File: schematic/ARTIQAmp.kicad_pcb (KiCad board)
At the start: 8 copper layers, 191 x 152.4 mm, 393 parts, among them IC1 LTC6090CS8E#PBF, IC10 LTC6090CS8E#PBF, IC11 LTC6090CS8E#PBF, IC12 LTC6090CS8E#PBF, IC13 LTC6090CS8E#PBF, IC14 LTC6090CS8E#PBF, IC15 LTC6090CS8E#PBF, IC16 LTC6090CS8E#PBF, IC17 LTC6090CS8E#PBF, IC18 LTC6090CS8E#PBF, IC19 LTC6090CS8E#PBF, IC2 LTC6090CS8E#PBF, IC20 LTC6090CS8E#PBF, IC21 LTC6090CS8E#PBF, IC22 LTC6090CS8E#PBF, IC23 LTC6090CS8E#PBF, IC24 LTC6090CS8E#PBF, IC25 LTC6090CS8E#PBF, IC26 LTC6090CS8E#PBF, IC27 LTC6090CS8E#PBF, IC28 LTC6090CS8E#PBF, IC29 LTC6090CS8E#PBF, IC3 LTC6090CS8E#PBF, IC30 LTC6090CS8E#PBF, IC31 LTC6090CS8E#PBF, IC32 LTC6090CS8E#PBF, IC4 LTC6090CS8E#PBF, IC5 LTC6090CS8E#PBF, IC6 LTC6090CS8E#PBF, IC7 LTC6090CS8E#PBF, IC8 LTC6090CS8E#PBF, IC9 LTC6090CS8E#PBF, J1 Power conneciton, J2 HD68, J3 HD68

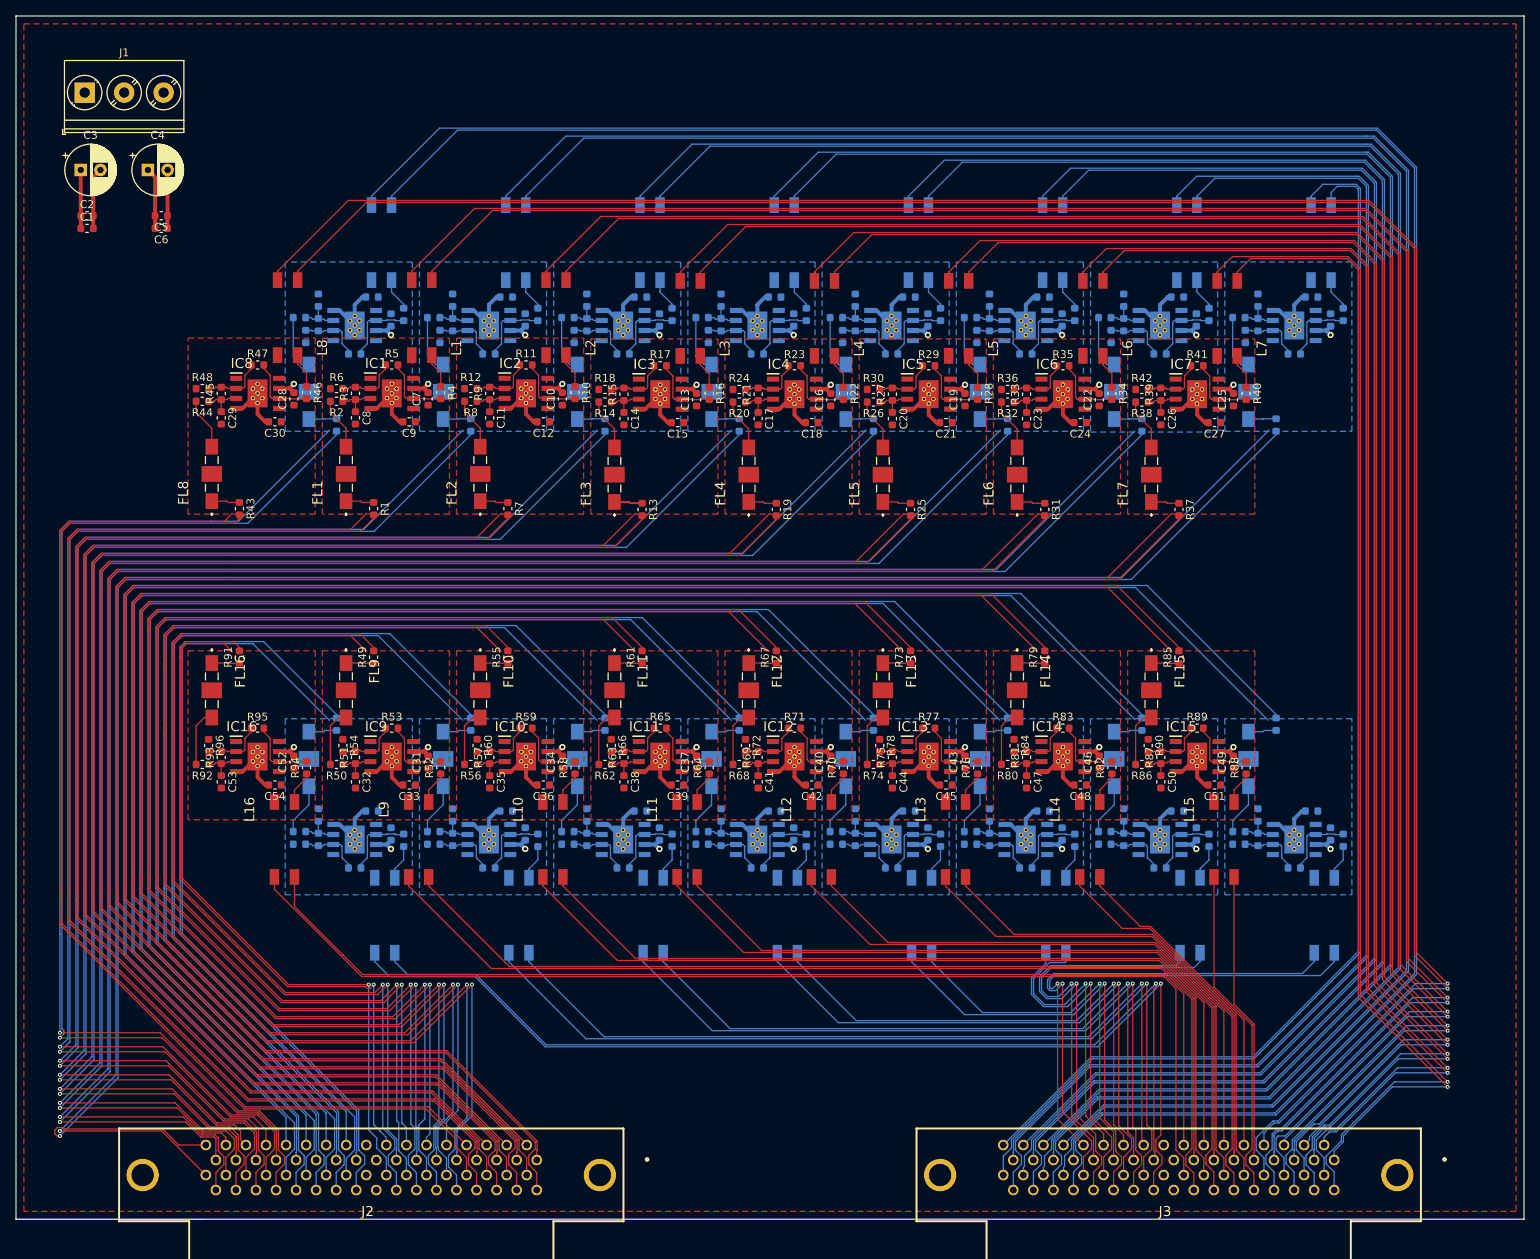
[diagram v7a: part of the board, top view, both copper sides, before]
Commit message: Board updates and starting to add more capacitors
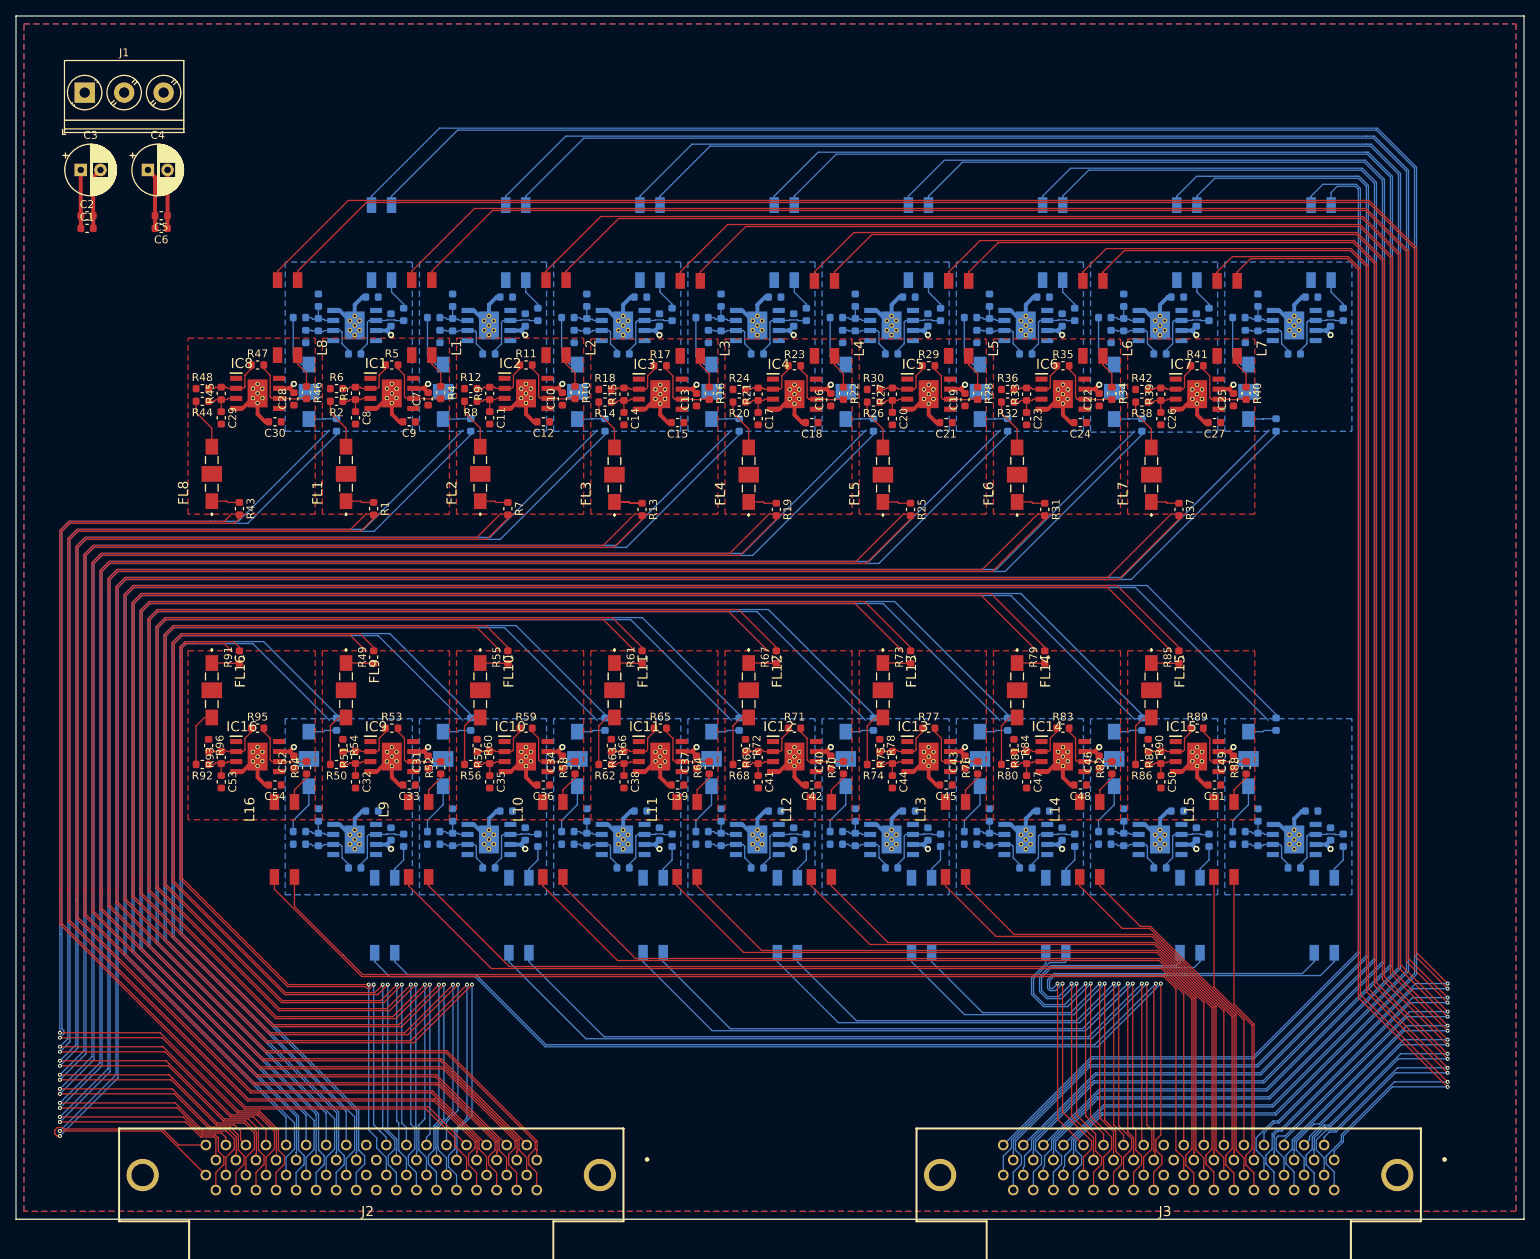
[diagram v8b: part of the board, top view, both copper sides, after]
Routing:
- added copper zone on B.Cu, net GND
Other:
- copper layers 8 -> 6
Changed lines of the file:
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@@
     (0 F.Cu signal)
     (1 In1.Cu power)
-    (2 In24.Cu signal)
-    (3 In2.Cu power)
-    (4 In3.Cu power)
-    (5 In54.Cu signal)
-    (6 In4.Cu power)
+    (2 In2.Cu power)
+    (3 In3.Cu power)
+    (4 In4.Cu power)
     (31 B.Cu signal)
     (32 B.Adhes user)
@@
   )
   (zone (net 198) (net_name /D25_IN_COM) (layer B.Cu) (hatch edge 0.508)
+    (priority 1)
     (connect_pads yes (clearance 0.254))
     (min_thickness 0.254)
@@
   )
   (zone (net 186) (net_name /D26_IN_COM) (layer B.Cu) (hatch edge 0.508)
+    (priority 1)
     (connect_pads yes (clearance 0.254))
     (min_thickness 0.254)
@@
   )
   (zone (net 187) (net_name /D27_IN_COM) (layer B.Cu) (hatch edge 0.508)
+    (priority 1)
     (connect_pads yes (clearance 0.254))
     (min_thickness 0.254)
@@
   )
   (zone (net 189) (net_name /D28_IN_COM) (layer B.Cu) (hatch edge 0.508)
+    (priority 1)
     (connect_pads yes (clearance 0.254))
     (min_thickness 0.254)
@@
   )
   (zone (net 191) (net_name /D29_IN_COM) (layer B.Cu) (hatch edge 0.508)
+    (priority 1)
     (connect_pads yes (clearance 0.254))
     (min_thickness 0.254)
@@
   )
   (zone (net 193) (net_name /D30_IN_COM) (layer B.Cu) (hatch edge 0.508)
+    (priority 1)
     (connect_pads yes (clearance 0.254))
     (min_thickness 0.254)
@@
   )
   (zone (net 194) (net_name /D31_IN_COM) (layer B.Cu) (hatch edge 0.508)
+    (priority 1)
     (connect_pads yes (clearance 0.254))
     (min_thickness 0.254)
@@
   )
   (zone (net 196) (net_name /D32_IN_COM) (layer B.Cu) (hatch edge 0.508)
+    (priority 1)
     (connect_pads yes (clearance 0.254))
     (min_thickness 0.254)
@@
   )
   (zone (net 184) (net_name /D17_IN_COM) (layer B.Cu) (hatch edge 0.508)
+    (priority 1)
     (connect_pads yes (clearance 0.254))
     (min_thickness 0.254)
@@
   )
   (zone (net 172) (net_name /D18_IN_COM) (layer B.Cu) (hatch edge 0.508)
+    (priority 1)
     (connect_pads yes (clearance 0.254))
     (min_thickness 0.254)
@@
   )
   (zone (net 173) (net_name /D19_IN_COM) (layer B.Cu) (hatch edge 0.508)
+    (priority 1)
     (connect_pads yes (clearance 0.254))
     (min_thickness 0.254)
@@
   )
   (zone (net 175) (net_name /D20_IN_COM) (layer B.Cu) (hatch edge 0.508)
+    (priority 1)
     (connect_pads yes (clearance 0.254))
     (min_thickness 0.254)
@@
   )
   (zone (net 177) (net_name /D21_IN_COM) (layer B.Cu) (hatch edge 0.508)
+    (priority 1)
     (connect_pads yes (clearance 0.254))
     (min_thickness 0.254)
@@
   )
   (zone (net 179) (net_name /D22_IN_COM) (layer B.Cu) (hatch edge 0.508)
+    (priority 1)
     (connect_pads yes (clearance 0.254))
     (min_thickness 0.254)
@@
   )
   (zone (net 180) (net_name /D23_IN_COM) (layer B.Cu) (hatch edge 0.508)
+    (priority 1)
     (connect_pads yes (clearance 0.254))
     (min_thickness 0.254)
@@
   )
   (zone (net 182) (net_name /D24_IN_COM) (layer B.Cu) (hatch edge 0.508)
+    (priority 1)
     (connect_pads yes (clearance 0.254))
     (min_thickness 0.254)
@@
     )
   )
+  (zone (net 1) (net_name GND) (layer F.Cu) (hatch edge 0.508)
+    (connect_pads yes (clearance 0.254))
+    (min_thickness 0.254)
+    (fill yes (arc_segments 32) (thermal_gap 0.508) (thermal_bridge_width 0.508))
+    (polygon
+      (pts
+        (xy 292.9 284.5) (xy 103.9 284.5) (xy 103.9 134.1) (xy 292.9 134.1)
+      )
+    )
+  )
   (zone (net 1) (net_name GND) (layer In4.Cu) (hatch edge 0.508)
     (connect_pads yes (clearance 0.508))
@@
     )
   )
-  (zone (net 1) (net_name GND) (layer F.Cu) (hatch edge 0.508)
+  (zone (net 1) (net_name GND) (layer B.Cu) (hatch edge 0.508)
     (connect_pads yes (clearance 0.254))
     (min_thickness 0.254)
